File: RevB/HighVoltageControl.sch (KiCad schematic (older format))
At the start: 15 parts, among them Q1 DMG2302U, U1 LMR14206, U7 AZ1117CR-3.3

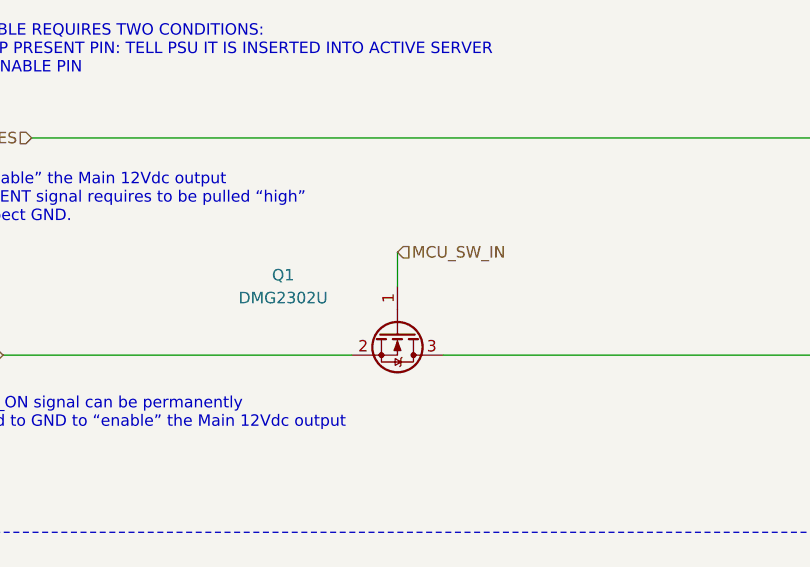
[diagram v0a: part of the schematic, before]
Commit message: update RevB design
- Corrected PSU_ON n-chan. Drain and Source swapped.
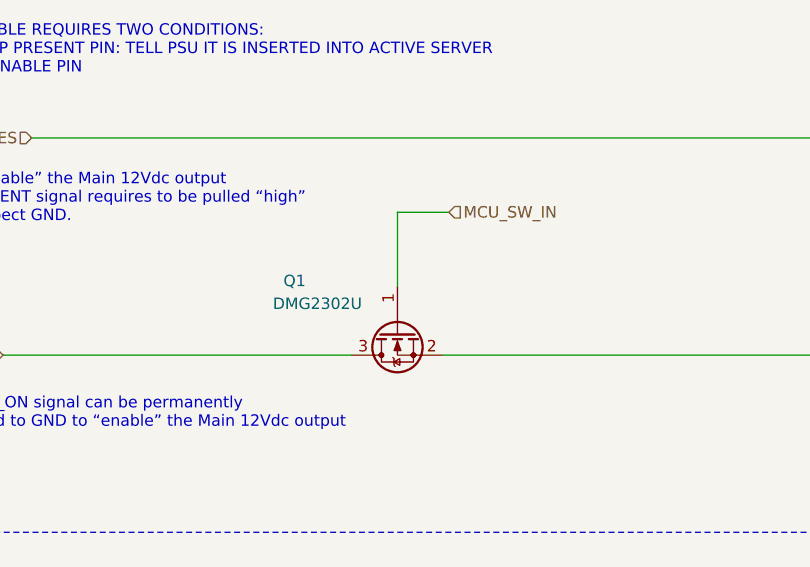
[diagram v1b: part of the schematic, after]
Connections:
- net GNDS: now also Q1.2 (S); no longer Q1.3 (D)
- net PSU_ON: now also Q1.3 (D); no longer Q1.2 (S)
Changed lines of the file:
@@
 U 1 1 5F001BDB
 P 5200 2675
-F 0 "Q1" V 4950 2175 50  0000 C CNN
-F 1 "DMG2302U" V 5050 2175 50  0000 C CNN
+F 0 "Q1" V 4975 3125 50  0000 C CNN
+F 1 "DMG2302U" V 5075 3025 50  0000 C CNN
 F 2 "Package_TO_SOT_SMD:SOT-23" H 5400 2600 50  0001 L CIN
 F 3 "http://www.diodes.com/assets/Datasheets/DMG2302U.pdf" H 5200 2675 50  0001 L CNN
 	1    5200 2675
-	0    1    1    0
-$EndComp
-Wire Wire Line
-	5200 2475 5200 2325
-Text HLabel 5200 2325 2    50   Input ~ 0
+	0    -1   1    0
+$EndComp
+Text HLabel 5425 2150 2    50   Input ~ 0
 MCU_SW_IN
 $Comp
@@
 Wire Notes Line
 	1000 3550 10675 3550
+Wire Wire Line
+	5425 2150 5200 2150
+Wire Wire Line
+	5200 2150 5200 2475
 $EndSCHEMATC

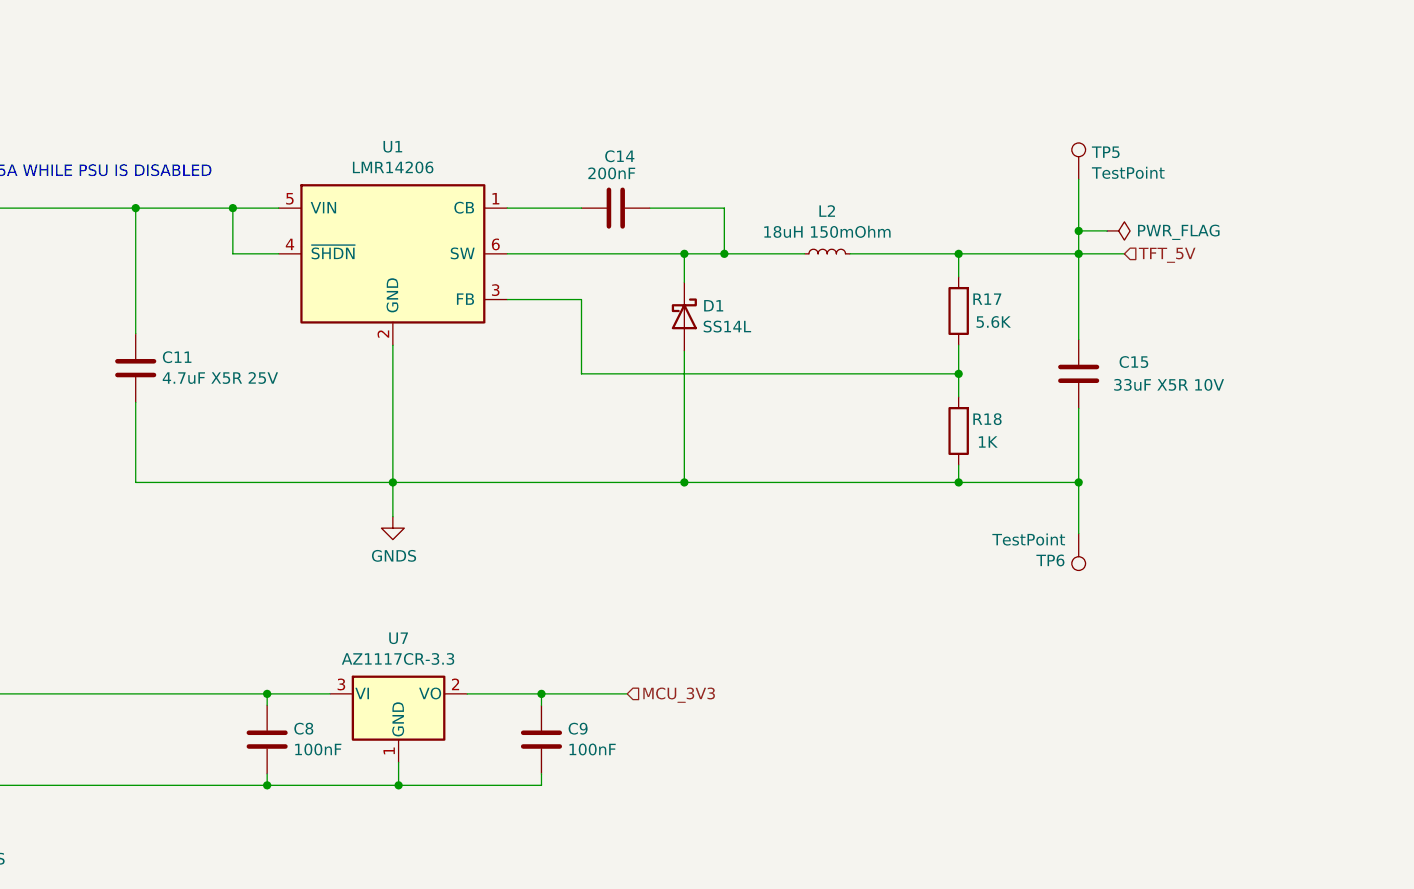
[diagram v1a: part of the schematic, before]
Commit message: updated revb
added missing pullup resistors
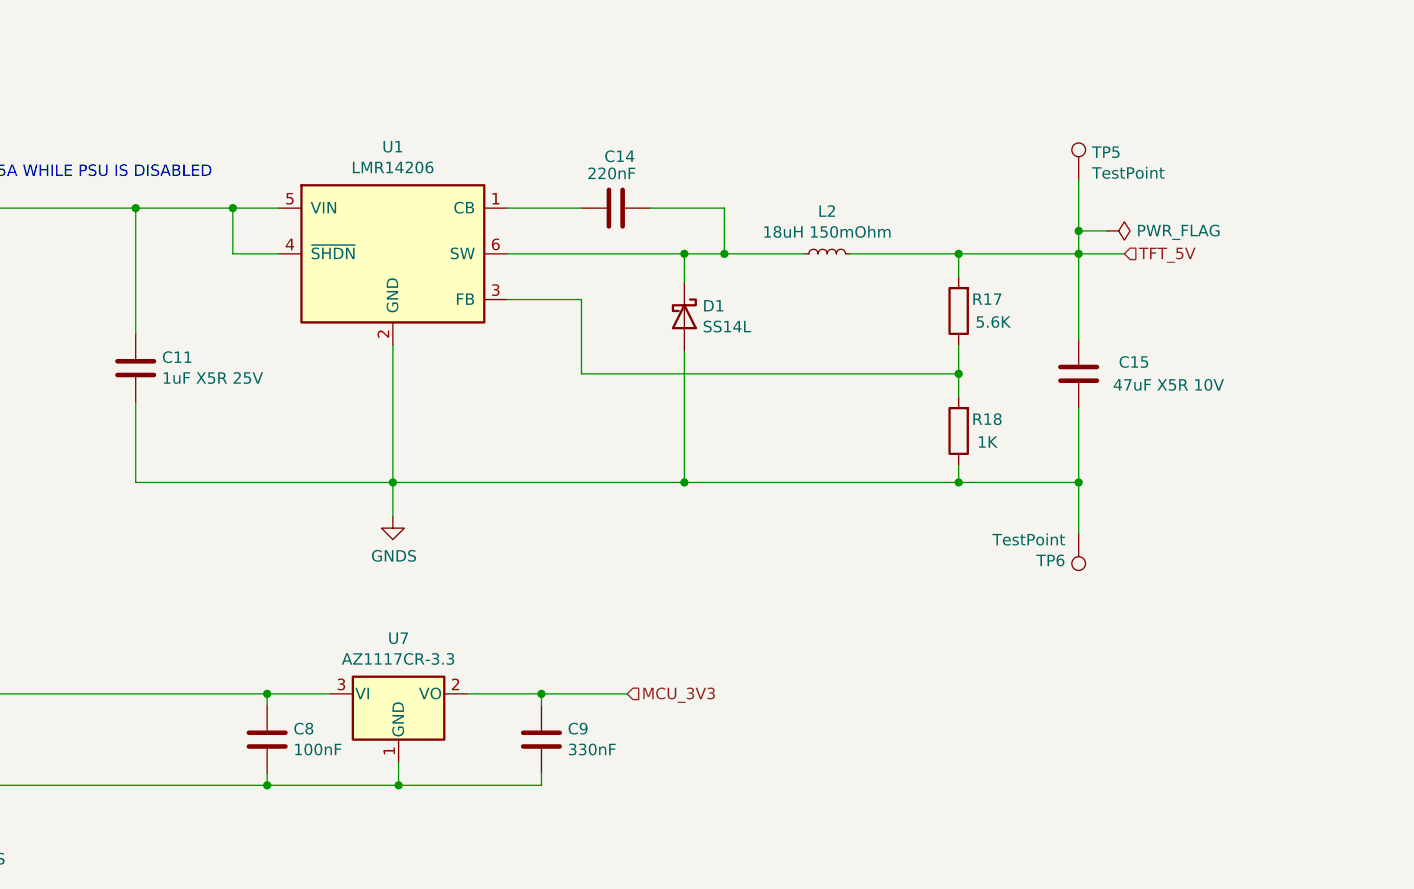
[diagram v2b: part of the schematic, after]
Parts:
- C11: value 4.7uF X5R 25V -> 1uF X5R 25V
- C14: value 200nF -> 220nF
- C15: value 33uF X5R 10V -> 47uF X5R 10V
- C9: value 100nF -> 330nF
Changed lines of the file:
@@
 P 5675 6950
 F 0 "C9" H 5790 6996 50  0000 L CNN
-F 1 "100nF" H 5790 6905 50  0000 L CNN
+F 1 "330nF" H 5790 6905 50  0000 L CNN
 F 2 "Capacitor_SMD:C_0805_2012Metric_Pad1.15x1.40mm_HandSolder" H 5713 6800 50  0001 C CNN
 F 3 "~" H 5675 6950 50  0001 C CNN
@@
 P 3900 5325
 F 0 "C11" H 4015 5371 50  0000 L CNN
-F 1 "4.7uF X5R 25V" H 4015 5280 50  0000 L CNN
+F 1 "1uF X5R 25V" H 4015 5280 50  0000 L CNN
 F 2 "Capacitor_SMD:C_0805_2012Metric_Pad1.15x1.40mm_HandSolder" H 3938 5175 50  0001 C CNN
 F 3 "~" H 3900 5325 50  0001 C CNN
@@
 P 6000 4625
 F 0 "C14" V 6225 4575 50  0000 L CNN
-F 1 "200nF" V 6150 4500 50  0000 L CNN
+F 1 "220nF" V 6150 4500 50  0000 L CNN
 F 2 "Capacitor_SMD:C_0805_2012Metric_Pad1.15x1.40mm_HandSolder" H 6038 4475 50  0001 C CNN
 F 3 "~" H 6000 4625 50  0001 C CNN
@@
 P 8025 5350
 F 0 "C15" H 8200 5300 50  0000 L CNN
-F 1 "33uF X5R 10V" H 8175 5400 50  0000 L CNN
+F 1 "47uF X5R 10V" H 8175 5400 50  0000 L CNN
 F 2 "Capacitor_SMD:C_0805_2012Metric_Pad1.15x1.40mm_HandSolder" H 8063 5200 50  0001 C CNN
 F 3 "~" H 8025 5350 50  0001 C CNN
